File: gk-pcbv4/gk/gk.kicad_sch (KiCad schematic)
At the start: 11 parts

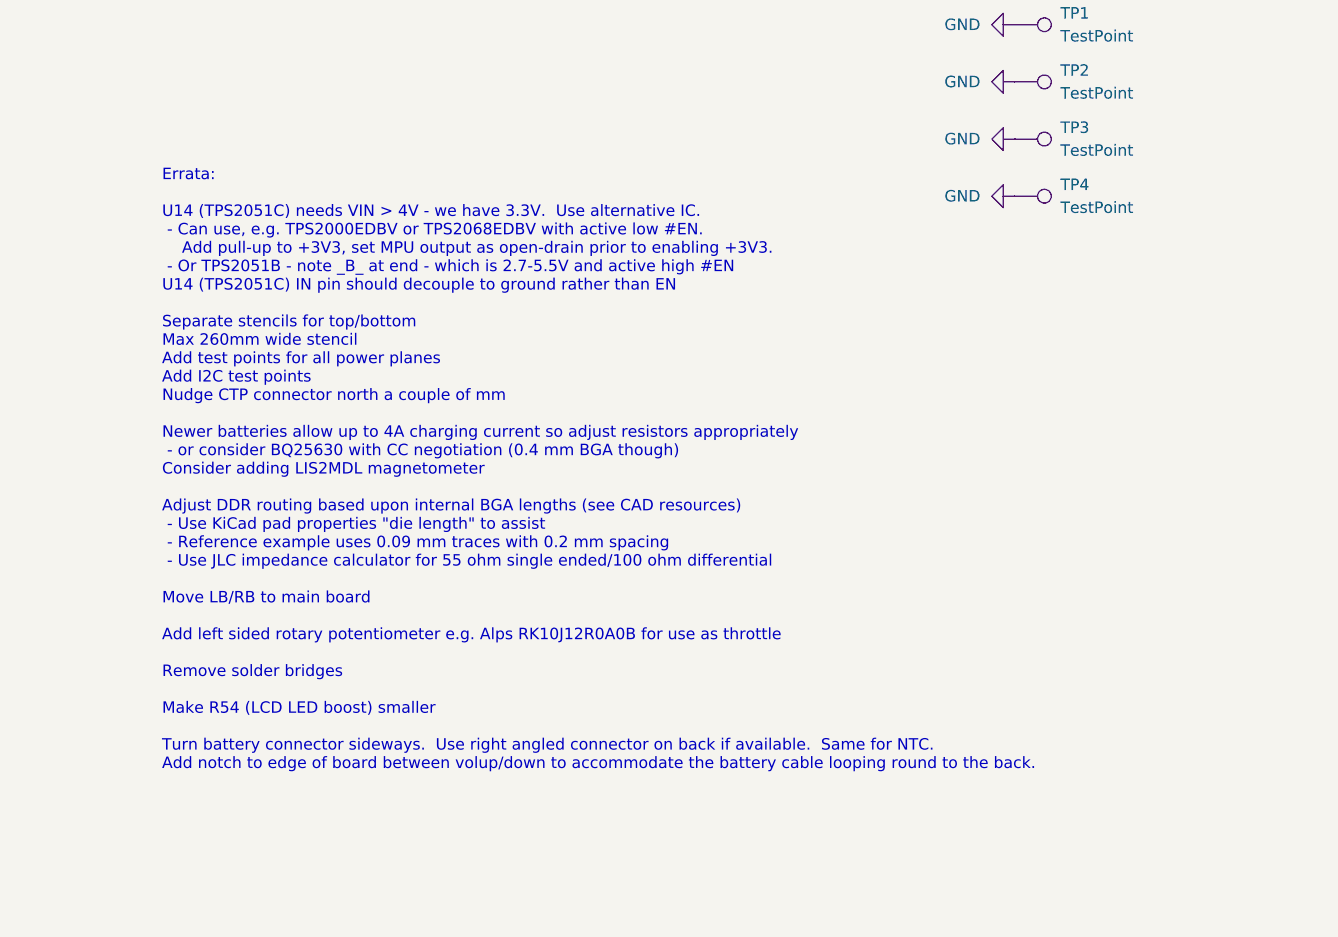
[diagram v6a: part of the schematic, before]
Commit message: fix tps2051 schematic
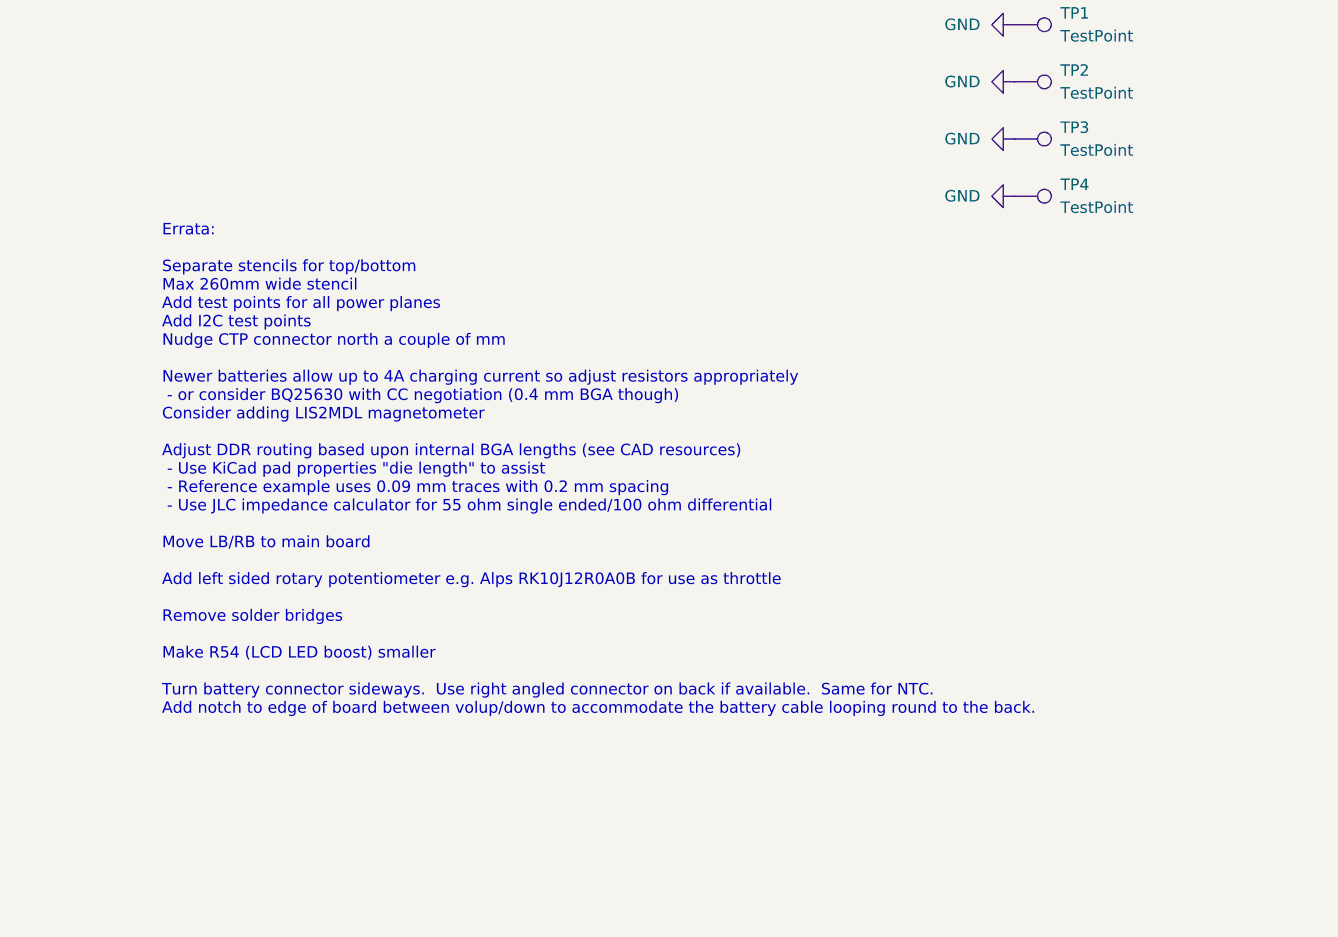
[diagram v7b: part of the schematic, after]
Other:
- note added: "Errata: Separate stencils for top/bottom Max 260mm wide stencil Add test points for all power planes Add I2C test points Nudge CTP connector north a couple of mm Newer batteries allow up to 4A charging current so adjust resistors appropriately - or consider BQ25630 with CC negotiation (0.4 mm BGA though) Consider adding LIS2MDL magnetometer Adjust DDR routing based upon internal BGA lengths (see 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"
- note removed: "Errata: U14 (TPS2051C) needs VIN > 4V - we have 3.3V. Use alternative IC. - Can use, e.g. TPS2000EDBV or TPS2068EDBV with active low #EN. Add pull-up to +3V3, set MPU output as open-drain prior to enabling +3V3. - Or TPS2051B - note _B_ at end - which is 2.7-5.5V and active high #EN U14 (TPS2051C) IN pin should decouple to ground rather than EN Separate stencils for top/bottom Max 260mm wide sten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"
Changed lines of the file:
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@@
 		)
 	)
-	(text "Errata:\n\nU14 (TPS2051C) needs VIN > 4V - we have 3.3V.  Use alternative IC.\n - Can use, e.g. TPS2000EDBV or TPS2068EDBV with active low #EN.\n    Add pull-up to +3V3, set MPU output as open-drain prior to enabling +3V3.\n - Or TPS2051B - note _B_ at end - which is 2.7-5.5V and active high #EN\nU14 (TPS2051C) IN pin should decouple to ground rather than EN\n\nSeparate stencils for top/bottom\nMax 260mm wide stencil\nAdd test points for all power planes\nAdd I2C test points\nNudge CTP connector north a couple of mm\n\nNewer batteries allow up to 4A charging current so adjust resistors appropriately\n - or consider BQ25630 with CC negotiation (0.4 mm BGA though)\nConsider adding LIS2MDL magnetometer\n\nAdjust DDR routing based upon internal BGA lengths (see CAD resources)\n - Use KiCad pad properties \"die length\" to assist\n - Reference example uses 0.09 mm traces with 0.2 mm spacing\n - Use JLC impedance calculator for 55 ohm single ended/100 ohm differential\n\nMove LB/RB to main board\n\nAdd left sided rotary potentiometer e.g. Alps RK10J12R0A0B for use as throttle\n\nRemove solder bridges\n\nMake R54 (LCD LED boost) smaller\n\nTurn battery connector sideways.  Use right angled connector on back if available.  Same for NTC.\nAdd notch to edge of board between volup/down to accommodate the battery cable looping round to the back.\n"
+	(text "Errata:\n\nSeparate stencils for top/bottom\nMax 260mm wide stencil\nAdd test points for all power planes\nAdd I2C test points\nNudge CTP connector north a couple of mm\n\nNewer batteries allow up to 4A charging current so adjust resistors appropriately\n - or consider BQ25630 with CC negotiation (0.4 mm BGA though)\nConsider adding LIS2MDL magnetometer\n\nAdjust DDR routing based upon internal BGA lengths (see CAD resources)\n - Use KiCad pad properties \"die length\" to assist\n - Reference example uses 0.09 mm traces with 0.2 mm spacing\n - Use JLC impedance calculator for 55 ohm single ended/100 ohm differential\n\nMove LB/RB to main board\n\nAdd left sided rotary potentiometer e.g. Alps RK10J12R0A0B for use as throttle\n\nRemove solder bridges\n\nMake R54 (LCD LED boost) smaller\n\nTurn battery connector sideways.  Use right angled connector on back if available.  Same for NTC.\nAdd notch to edge of board between volup/down to accommodate the battery cable looping round to the back.\n"
 		(exclude_from_sim no)
 		(at 104.648 80.01 0)

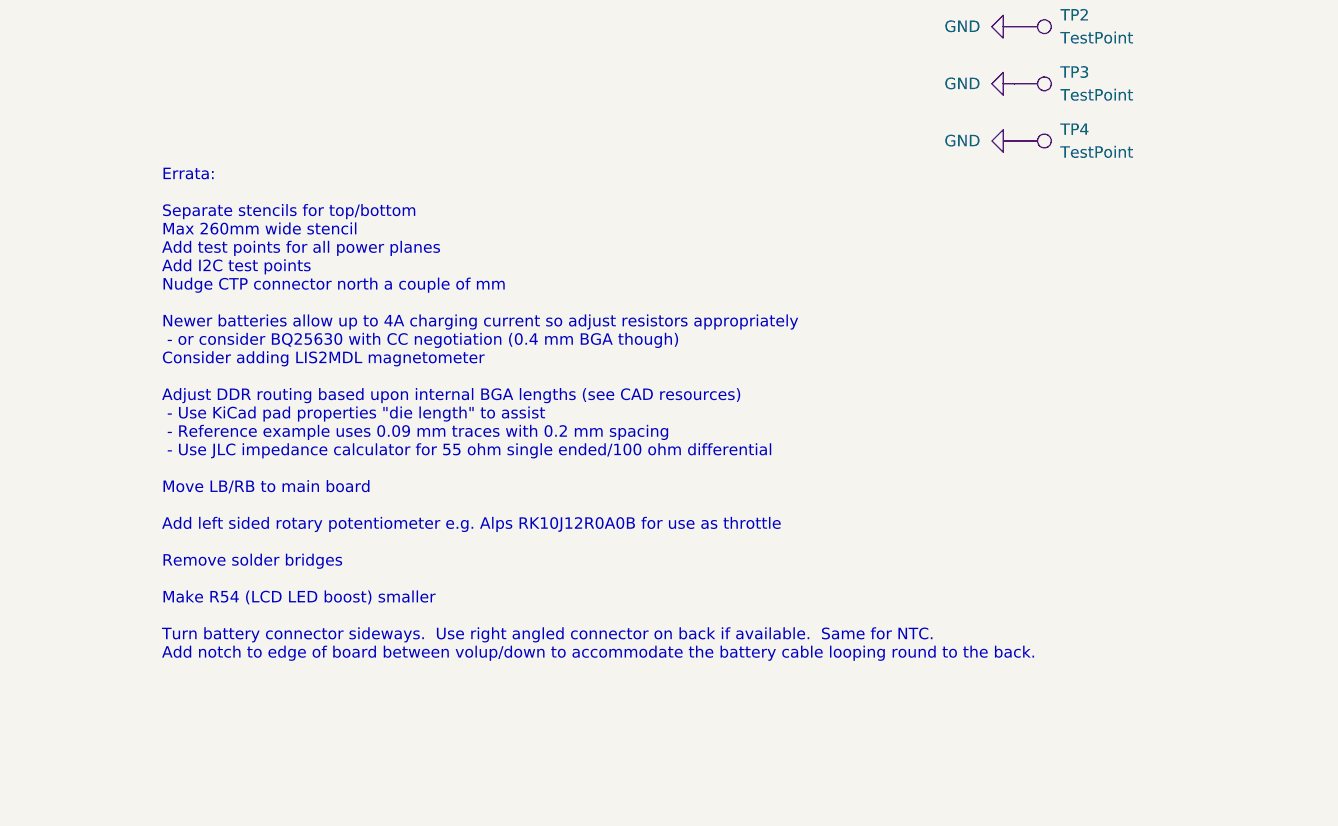
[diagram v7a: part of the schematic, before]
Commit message: add magnetometer
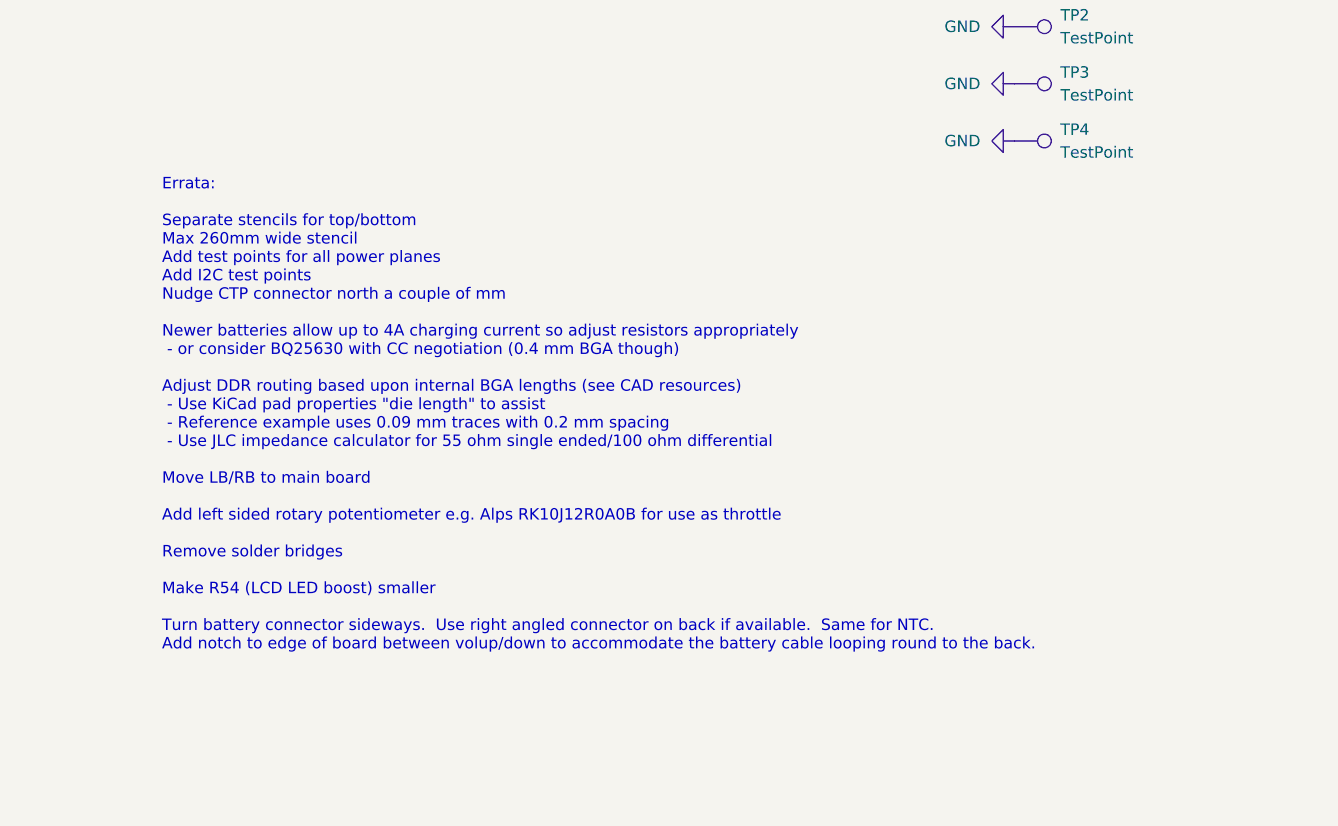
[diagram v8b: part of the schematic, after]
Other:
- note added: "Errata: Separate stencils for top/bottom Max 260mm wide stencil Add test points for all power planes Add I2C test points Nudge CTP connector north a couple of mm Newer batteries allow up to 4A charging current so adjust resistors appropriately - or consider BQ25630 with CC negotiation (0.4 mm BGA though) Adjust DDR routing based upon internal BGA lengths (see CAD resources) - Use KiCad pad proper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"
- note removed: "Errata: Separate stencils for top/bottom Max 260mm wide stencil Add test points for all power planes Add I2C test points Nudge CTP connector north a couple of mm Newer batteries allow up to 4A charging current so adjust resistors appropriately - or consider BQ25630 with CC negotiation (0.4 mm BGA though) Consider adding LIS2MDL magnetometer Adjust DDR routing based upon internal BGA lengths (see 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"
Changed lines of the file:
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@@
 		)
 	)
-	(text "Errata:\n\nSeparate stencils for top/bottom\nMax 260mm wide stencil\nAdd test points for all power planes\nAdd I2C test points\nNudge CTP connector north a couple of mm\n\nNewer batteries allow up to 4A charging current so adjust resistors appropriately\n - or consider BQ25630 with CC negotiation (0.4 mm BGA though)\nConsider adding LIS2MDL magnetometer\n\nAdjust DDR routing based upon internal BGA lengths (see CAD resources)\n - Use KiCad pad properties \"die length\" to assist\n - Reference example uses 0.09 mm traces with 0.2 mm spacing\n - Use JLC impedance calculator for 55 ohm single ended/100 ohm differential\n\nMove LB/RB to main board\n\nAdd left sided rotary potentiometer e.g. Alps RK10J12R0A0B for use as throttle\n\nRemove solder bridges\n\nMake R54 (LCD LED boost) smaller\n\nTurn battery connector sideways.  Use right angled connector on back if available.  Same for NTC.\nAdd notch to edge of board between volup/down to accommodate the battery cable looping round to the back.\n"
+	(text "Errata:\n\nSeparate stencils for top/bottom\nMax 260mm wide stencil\nAdd test points for all power planes\nAdd I2C test points\nNudge CTP connector north a couple of mm\n\nNewer batteries allow up to 4A charging current so adjust resistors appropriately\n - or consider BQ25630 with CC negotiation (0.4 mm BGA though)\n\nAdjust DDR routing based upon internal BGA lengths (see CAD resources)\n - Use KiCad pad properties \"die length\" to assist\n - Reference example uses 0.09 mm traces with 0.2 mm spacing\n - Use JLC impedance calculator for 55 ohm single ended/100 ohm differential\n\nMove LB/RB to main board\n\nAdd left sided rotary potentiometer e.g. Alps RK10J12R0A0B for use as throttle\n\nRemove solder bridges\n\nMake R54 (LCD LED boost) smaller\n\nTurn battery connector sideways.  Use right angled connector on back if available.  Same for NTC.\nAdd notch to edge of board between volup/down to accommodate the battery cable looping round to the back.\n"
 		(exclude_from_sim no)
 		(at 104.648 80.01 0)
